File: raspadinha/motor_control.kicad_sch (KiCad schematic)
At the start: 5 parts, among them M3 Motor_DC, Q3 IRF640N

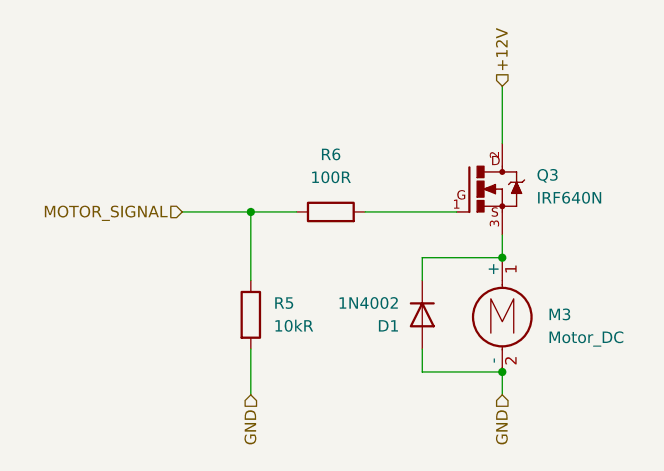
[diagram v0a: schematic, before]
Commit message: feat: usando o mosfet IRFZ44N feat: switch de on/off na fonte de alimentação
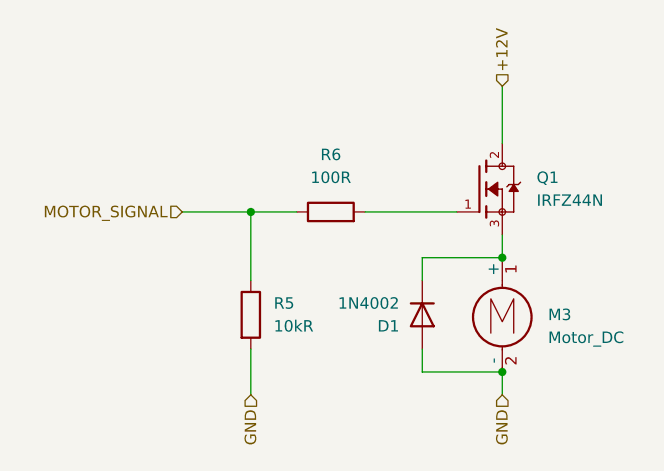
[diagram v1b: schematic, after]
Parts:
- removed Q3: IRF640N, symbol IRF640N:IRF640N
- added Q1: IRFZ44N, IRFZ44N:TO254P1016X419X2286-3, symbol IRFZ44N:IRFZ44N
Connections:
- net +12V: now also Q1.2
- net at D1.1 (K), M3.1 (+): now also Q1.3
- net at R6.2: now also Q1.1
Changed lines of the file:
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@@
-	)
-	(symbol
-		(lib_id "IRF640N:IRF640N")
-		(at 162.56 90.17 0)
-		(unit 1)
-		(exclude_from_sim no)
-		(in_bom yes)
-		(on_board yes)
-		(dnp no)
-		(fields_autoplaced yes)
-		(property "Reference" "Q3"
-			(at 168.91 88.6377 0)
-			(effects
-				(font
-					(size 1.27 1.27)
-				)
-				(justify left)
-			)
-		)
-		(property "Value" "IRF640N"
-			(at 168.91 91.1777 0)
-			(effects
-				(font
-					(size 1.27 1.27)
-				)
-				(justify left)
-			)
-		)
-		(property "Footprint" ""
-			(at 162.56 90.17 0)
-			(effects
-				(font
-					(size 1.27 1.27)
-				)
-				(hide yes)
-			)
-		)
-		(property "Datasheet" ""
-			(at 162.56 90.17 0)
-			(effects
-				(font
-					(size 1.27 1.27)
-				)
-				(hide yes)
-			)
-		)
-		(property "Description" ""
-			(at 162.56 90.17 0)
-			(effects
-				(font
-					(size 1.27 1.27)
-				)
-				(hide yes)
-			)
-		)
-		(property "MF" "Infineon Technologies"
-			(at 162.56 90.17 0)
-			(effects
-				(font
-					(size 1.27 1.27)
-				)
-				(justify bottom)
-				(hide yes)
-			)
-		)
-		(property "Description_1" "N-Channel 200V 18A (Tc) 150W (Tc) Through Hole TO-220AB"
-			(at 162.56 90.17 0)
-			(effects
-				(font
-					(size 1.27 1.27)
-				)
-				(justify bottom)
-				(hide yes)
-			)
-		)
-		(property "Package" "TO-263-3 Infineon Technologies"
-			(at 162.56 90.17 0)
-			(effects
-				(font
-					(size 1.27 1.27)
-				)
-				(justify bottom)
-				(hide yes)
-			)
-		)
-		(property "Price" "None"
-			(at 162.56 90.17 0)
-			(effects
-				(font
-					(size 1.27 1.27)
-				)
-				(justify bottom)
-				(hide yes)
-			)
-		)
-		(property "SnapEDA_Link" "https://www.snapeda.com/parts/IRF640N/Infineon/view-part/?ref=snap"
-			(at 162.56 90.17 0)
-			(effects
-				(font
-					(size 1.27 1.27)
-				)
-				(justify bottom)
-				(hide yes)
-			)
-		)
-		(property "MP" "IRF640N"
-			(at 162.56 90.17 0)
-			(effects
-				(font
-					(size 1.27 1.27)
-				)
-				(justify bottom)
-				(hide yes)
-			)
-		)
-		(property "Availability" "Not in stock"
-			(at 162.56 90.17 0)
-			(effects
-				(font
-					(size 1.27 1.27)
-				)
-				(justify bottom)
-				(hide yes)
-			)
-		)
-		(property "Check_prices" "https://www.snapeda.com/parts/IRF640N/Infineon/view-part/?ref=eda"
-			(at 162.56 90.17 0)
-			(effects
-				(font
-					(size 1.27 1.27)
-				)
-				(justify bottom)
-				(hide yes)
-			)
-		)
-		(pin "3"
-		)
-		(pin "2"
-		)
-		(pin "1"
-		)
-		(instances
-			(project "raspadinha"
-				(path "/0ce4bf39-76b0-428c-8682-47e2500753cc/7e5f2161-e419-4edf-867f-a791766c9953"
-					(reference "Q3")
-					(unit 1)
-				)
-			)
-		)
 	)
 	(symbol
@@
 					(unit 1)
 				)
+			)
+		)
+	)
+	(symbol
+		(lib_id "IRFZ44N:IRFZ44N")
+		(at 162.56 90.17 0)
+		(unit 1)
+		(exclude_from_sim no)
+		(in_bom yes)
+		(on_board yes)
+		(dnp no)
+		(fields_autoplaced yes)
+		(property "Reference" "Q1"
+			(at 168.91 88.8999 0)
+			(effects
+				(font
+					(size 1.27 1.27)
+				)
+				(justify left)
+			)
+		)
+		(property "Value" "IRFZ44N"
+			(at 168.91 91.4399 0)
+			(effects
+				(font
+					(size 1.27 1.27)
+				)
+				(justify left)
+			)
+		)
+		(property "Footprint" "IRFZ44N:TO254P1016X419X2286-3"
+			(at 162.56 90.17 0)
+			(effects
+				(font
+					(size 1.27 1.27)
+				)
+				(justify bottom)
+				(hide yes)
+			)
+		)
+		(property "Datasheet" ""
+			(at 162.56 90.17 0)
+			(effects
+				(font
+					(size 1.27 1.27)
+				)
+				(hide yes)
+			)
+		)
+		(property "Description" ""
+			(at 162.56 90.17 0)
+			(effects
+				(font
+					(size 1.27 1.27)
+				)
+				(hide yes)
+			)
+		)
+		(property "MF" "Infineon Technologies"
+			(at 162.56 90.17 0)
+			(effects
+				(font
+					(size 1.27 1.27)
+				)
+				(justify bottom)
+				(hide yes)
+			)
+		)
+		(property "MAXIMUM_PACKAGE_HEIGHT" "22.86 mm"
+			(at 162.56 90.17 0)
+			(effects
+				(font
+					(size 1.27 1.27)
+				)
+				(justify bottom)
+				(hide yes)
+			)
+		)
+		(property "Package" "TO-220AB-3 Infineon"
+			(at 162.56 90.17 0)
+			(effects
+				(font
+					(size 1.27 1.27)
+				)
+				(justify bottom)
+				(hide yes)
+			)
+		)
+		(property "Price" "None"
+			(at 162.56 90.17 0)
+			(effects
+				(font
+					(size 1.27 1.27)
+				)
+				(justify bottom)
+				(hide yes)
+			)
+		)
+		(property "Check_prices" "https://www.snapeda.com/parts/IRFZ44N/Infineon/view-part/?ref=eda"
+			(at 162.56 90.17 0)
+			(effects
+				(font
+					(size 1.27 1.27)
+				)
+				(justify bottom)
+				(hide yes)
+			)
+		)
+		(property "STANDARD" "IPC 7351B"
+			(at 162.56 90.17 0)
+			(effects
+				(font
+					(size 1.27 1.27)
+				)
+				(justify bottom)
+				(hide yes)
+			)
+		)
+		(property "PARTREV" "09/21/10"
+			(at 162.56 90.17 0)
+			(effects
+				(font
+					(size 1.27 1.27)
+				)
+				(justify bottom)
+				(hide yes)
+			)
+		)
+		(property "SnapEDA_Link" "https://www.snapeda.com/parts/IRFZ44N/Infineon/view-part/?ref=snap"
+			(at 162.56 90.17 0)
+			(effects
+				(font
+					(size 1.27 1.27)
+				)
+				(justify bottom)
+				(hide yes)
+			)
+		)
+		(property "MP" "IRFZ44N"
+			(at 162.56 90.17 0)
+			(effects
+				(font
+					(size 1.27 1.27)
+				)
+				(justify bottom)
+				(hide yes)
+			)
+		)
+		(property "Description_1" "N-Channel 55 V 49A (Tc) 94W (Tc) Through Hole TO-220AB"
+			(at 162.56 90.17 0)
+			(effects
+				(font
+					(size 1.27 1.27)
+				)
+				(justify bottom)
+				(hide yes)
+			)
+		)
+		(property "SNAPEDA_PN" "IRFZ44N"
+			(at 162.56 90.17 0)
+			(effects
+				(font
+					(size 1.27 1.27)
+				)
+				(justify bottom)
+				(hide yes)
+			)
+		)
+		(property "Availability" "In Stock"
+			(at 162.56 90.17 0)
+			(effects
+				(font
+					(size 1.27 1.27)
+				)
+				(justify bottom)
+				(hide yes)
+			)
+		)
+		(property "MANUFACTURER" "Infineon"
+			(at 162.56 90.17 0)
+			(effects
+				(font
+					(size 1.27 1.27)
+				)
+				(justify bottom)
+				(hide yes)
+			)
+		)
+		(pin "1"
+		)
+		(pin "2"
+		)
+		(pin "3"
+		)
+		(instances
+			(project ""
+				(path "/0ce4bf39-76b0-428c-8682-47e2500753cc/7e5f2161-e419-4edf-867f-a791766c9953"
+					(reference "Q1")
+					(unit 1)
+				)

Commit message: feat: Os Footprint foram todos atribuidos fix: A placa da Esp32 foi trocada pela que temos disponível
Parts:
- M3: footprint (none) -> TerminalBlock_Phoenix:TerminalBlock_Phoenix_PT-1,5-2-3.5-H_1x02_P3.50mm_Horizontal
- R5, R6: footprint (none) -> Resistor_THT:R_Axial_DIN0411_L9.9mm_D3.6mm_P12.70mm_Horizontal
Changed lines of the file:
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@@
 		(title "Geladinho, Motor control")
 		(date "2025-11-20")
-		(rev "v1.0.0")
+		(rev "v1.1.0")
 		(company "Universidade Federal Do Ceará")
 	)
@@
 			)
 		)
-		(property "Footprint" ""
+		(property "Footprint" "TerminalBlock_Phoenix:TerminalBlock_Phoenix_PT-1,5-2-3.5-H_1x02_P3.50mm_Horizontal"
 			(at 165.1 105.156 0)
 			(effects
@@
 			)
 		)
-		(property "Footprint" ""
+		(property "Footprint" "Resistor_THT:R_Axial_DIN0411_L9.9mm_D3.6mm_P12.70mm_Horizontal"
 			(at 135.382 104.14 90)
 			(effects
@@
 			)
 		)
-		(property "Footprint" ""
+		(property "Footprint" "Resistor_THT:R_Axial_DIN0411_L9.9mm_D3.6mm_P12.70mm_Horizontal"
 			(at 146.05 94.488 90)
 			(effects

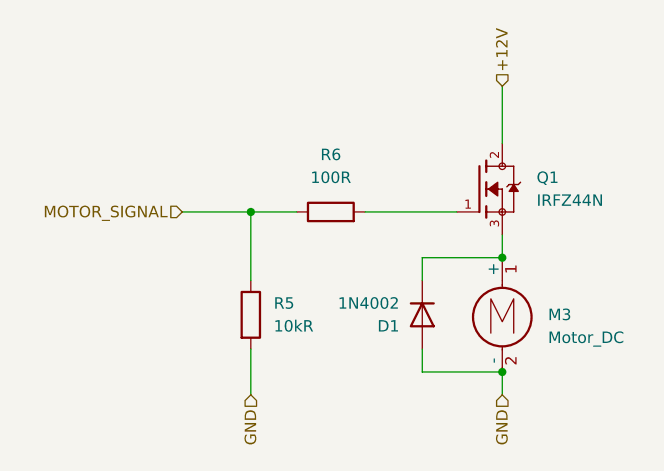
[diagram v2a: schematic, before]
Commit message: feat: Refatoração da alimentação da placa feat: Renomeação do número dos componentes
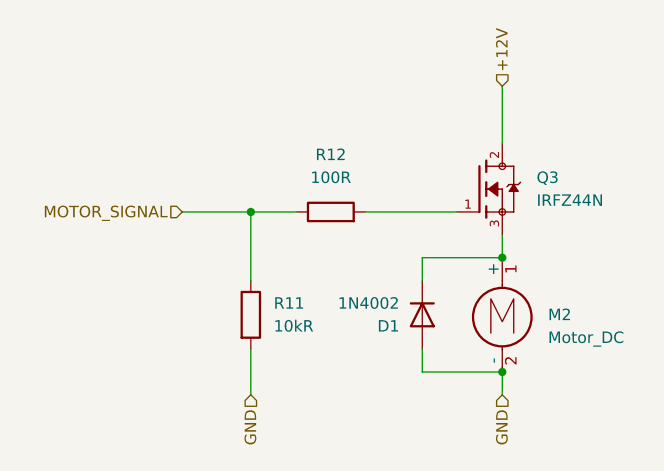
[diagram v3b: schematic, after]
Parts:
- renumbered M3 to M2, Q1 to Q3, R5 to R11, R6 to R12
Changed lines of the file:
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@@
 		(dnp no)
 		(fields_autoplaced yes)
-		(property "Reference" "M3"
+		(property "Reference" "M2"
 			(at 170.18 104.1399 0)
 			(effects
@@
 			(project "raspadinha"
 				(path "/0ce4bf39-76b0-428c-8682-47e2500753cc/7e5f2161-e419-4edf-867f-a791766c9953"
-					(reference "M3")
+					(reference "M2")
 					(unit 1)
 				)
@@
 		(dnp no)
 		(fields_autoplaced yes)
-		(property "Reference" "R5"
+		(property "Reference" "R11"
 			(at 139.7 102.8699 0)
 			(effects
@@
 			(project "raspadinha"
 				(path "/0ce4bf39-76b0-428c-8682-47e2500753cc/7e5f2161-e419-4edf-867f-a791766c9953"
-					(reference "R5")
+					(reference "R11")
 					(unit 1)
 				)
@@
 		(dnp no)
 		(fields_autoplaced yes)
-		(property "Reference" "Q1"
+		(property "Reference" "Q3"
 			(at 168.91 88.8999 0)
 			(effects
@@
 			(project ""
 				(path "/0ce4bf39-76b0-428c-8682-47e2500753cc/7e5f2161-e419-4edf-867f-a791766c9953"
-					(reference "Q1")
+					(reference "Q3")
 					(unit 1)
 				)
@@
 		(dnp no)
 		(fields_autoplaced yes)
-		(property "Reference" "R6"
+		(property "Reference" "R12"
 			(at 146.05 86.36 90)
 			(effects
@@
 			(project "raspadinha"
 				(path "/0ce4bf39-76b0-428c-8682-47e2500753cc/7e5f2161-e419-4edf-867f-a791766c9953"
-					(reference "R6")
+					(reference "R12")
 					(unit 1)
 				)
